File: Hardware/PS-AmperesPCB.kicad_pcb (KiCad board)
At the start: 2 copper layers, 70 x 60 mm, 45 parts, among them J1 Conn_01x04, J2 PeripheralCANConnector, J3 PeripheralCANConnector, U1 PeripheralSOM, U2 INA145UA/2K5, U3 AMC1300BDWV, U4 RO-123.3S_HP

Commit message: lay out lay out
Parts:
- removed +12V1, +3V3, +3V3H1, GND1, GNDH1, GNDPWR1, INN1, INP1, OUTN1, OUTP1, VOut1, aOut1: TestPoint, TestPoint:TestPoint_Keystone_5005-5009_Compact
- removed LOGO2: solarlogo, UTSVT_Special:UTSVT_Logo_Symbol
- removed REF**: Symbol_HighVoltage_Small, UTSVT_Special:Symbol_HighVoltage_Small
- added C11: 10uF, Capacitor_SMD:C_0805_2012Metric_Pad1.18x1.45mm_HandSolder, F.Cu at (99.9, 103.1)
- added C12: 10nF, Capacitor_SMD:C_0603_1608Metric_Pad1.08x0.95mm_HandSolder, F.Cu at (96.3, 101.0)
- added C13: 3.3nF, Capacitor_SMD:C_0603_1608Metric_Pad1.08x0.95mm_HandSolder, F.Cu at (108.7, 98.0)
- added C14: 0.1uF, Capacitor_SMD:C_0603_1608Metric_Pad1.08x0.95mm_HandSolder, F.Cu at (95.8, 111.8)
- added C15: 0.1uF, Capacitor_SMD:C_0603_1608Metric_Pad1.08x0.95mm_HandSolder, F.Cu at (96.6, 106.5)
- added C16: 1uF, Capacitor_SMD:C_0603_1608Metric_Pad1.08x0.95mm_HandSolder, F.Cu at (95.8, 109.0)
- added C17: 10uF, Capacitor_SMD:C_0805_2012Metric_Pad1.18x1.45mm_HandSolder, F.Cu at (101.9, 109.2)
- added C18: 10uF, Capacitor_SMD:C_0805_2012Metric_Pad1.18x1.45mm_HandSolder, F.Cu at (101.9, 113.5)
- added C19: 4.7uF, Capacitor_SMD:C_0805_2012Metric_Pad1.18x1.45mm_HandSolder, F.Cu at (106.7, 140.6)
- added C20: 100nF, Capacitor_SMD:C_0603_1608Metric_Pad1.08x0.95mm_HandSolder, F.Cu at (104.1, 140.7)
- added C21: 100nF, Capacitor_SMD:C_0603_1608Metric_Pad1.08x0.95mm_HandSolder, F.Cu at (101.6, 140.7)
- added C22: 100nF, Capacitor_SMD:C_0603_1608Metric_Pad1.08x0.95mm_HandSolder, F.Cu at (99.1, 140.7)
- added C23: 100nF, Capacitor_SMD:C_0603_1608Metric_Pad1.08x0.95mm_HandSolder, F.Cu at (88.5, 140.2)
- added C24: 100nF, Capacitor_SMD:C_0603_1608Metric_Pad1.08x0.95mm_HandSolder, F.Cu at (88.5, 141.9)
- added C25: 12p, Capacitor_SMD:C_0603_1608Metric_Pad1.08x0.95mm_HandSolder, F.Cu at (83.8, 133.7)
- added C26: 100nF, Capacitor_SMD:C_0603_1608Metric_Pad1.08x0.95mm_HandSolder, F.Cu at (88.5, 145.5)
- added C27: 12p, Capacitor_SMD:C_0603_1608Metric_Pad1.08x0.95mm_HandSolder, F.Cu at (83.8, 137.1)
- added C28: 100nF, Capacitor_SMD:C_0603_1608Metric_Pad1.08x0.95mm_HandSolder, F.Cu at (105.8, 148.5)
- added C29: 0.1uF, Capacitor_SMD:C_0603_1608Metric_Pad1.08x0.95mm_HandSolder, F.Cu at (95.2, 117.9)
- added C30: 100nF, Capacitor_SMD:C_0603_1608Metric_Pad1.08x0.95mm_HandSolder, F.Cu at (84.8, 127.8)
- added C31: 100nF, Capacitor_SMD:C_0603_1608Metric_Pad1.08x0.95mm_HandSolder, F.Cu at (86.6, 127.8)
- added C32: 4.7uF, Capacitor_SMD:C_0805_2012Metric_Pad1.18x1.45mm_HandSolder, F.Cu at (111.1, 118.6)
- added C33: 0.1uF, Capacitor_SMD:C_0603_1608Metric_Pad1.08x0.95mm_HandSolder, F.Cu at (104.5, 118.8)
- added C34: 10uF, Capacitor_SMD:C_0805_2012Metric_Pad1.18x1.45mm_HandSolder, F.Cu at (101.7, 117.9)
- added C35: 4.7uF, Capacitor_SMD:C_0805_2012Metric_Pad1.18x1.45mm_HandSolder, F.Cu at (105.5, 121.9)
- added C36: 0.1uF, Capacitor_SMD:C_0603_1608Metric_Pad1.08x0.95mm_HandSolder, F.Cu at (107.1, 118.8)
- added C37: 0.1uF, Capacitor_SMD:C_0603_1608Metric_Pad1.08x0.95mm_HandSolder, F.Cu at (100.1, 64.1)
- added C38: 1uF, Capacitor_SMD:C_0603_1608Metric_Pad1.08x0.95mm_HandSolder, F.Cu at (102.6, 64.1)
- added C39: 10uF, Capacitor_SMD:C_0805_2012Metric_Pad1.18x1.45mm_HandSolder, F.Cu at (112.0, 64.2)
- added C40: 0.1uF, Capacitor_SMD:C_0603_1608Metric_Pad1.08x0.95mm_HandSolder, F.Cu at (109.5, 64.1)
- added C41: 1uF, Capacitor_SMD:C_0603_1608Metric_Pad1.08x0.95mm_HandSolder, F.Cu at (124.5, 76.9)
- added C42: 0.1uF, Capacitor_SMD:C_0603_1608Metric_Pad1.08x0.95mm_HandSolder, F.Cu at (124.2, 64.4)
- added C43: 1nF, Capacitor_SMD:C_0603_1608Metric_Pad1.08x0.95mm_HandSolder, F.Cu at (126.4, 68.7)
- added C44: 7.5uF, Capacitor_SMD:C_0603_1608Metric_Pad1.08x0.95mm_HandSolder, F.Cu at (120.7, 76.9)
- added C45: 100nF, Capacitor_SMD:C_0603_1608Metric_Pad1.08x0.95mm_HandSolder, F.Cu at (128.9, 72.3)
- added C46: 1uF, Capacitor_SMD:C_0603_1608Metric_Pad1.08x0.95mm_HandSolder, F.Cu at (126.4, 72.3)
- added C47: 1uF, Capacitor_SMD:C_0603_1608Metric_Pad1.08x0.95mm_HandSolder, F.Cu at (110.7, 72.6)
- added C48: 100nF, Capacitor_SMD:C_0603_1608Metric_Pad1.08x0.95mm_HandSolder, F.Cu at (108.2, 72.6)
- added C49: 0.1uF, Capacitor_SMD:C_0603_1608Metric_Pad1.08x0.95mm_HandSolder, F.Cu at (131.2, 77.7)
- added C50: 10uF, Capacitor_SMD:C_0805_2012Metric_Pad1.18x1.45mm_HandSolder, F.Cu at (83.8, 91.7)
- added C51: 1uF, Capacitor_SMD:C_0603_1608Metric_Pad1.08x0.95mm_HandSolder, F.Cu at (83.5, 93.7)
- added C52: 1uF, Capacitor_SMD:C_0603_1608Metric_Pad1.08x0.95mm_HandSolder, F.Cu at (88.0, 91.4)
- added C53: 10uF, Capacitor_SMD:C_0805_2012Metric_Pad1.18x1.45mm_HandSolder, F.Cu at (87.9, 93.5)
- added C54: 100nF, Capacitor_SMD:C_0603_1608Metric_Pad1.08x0.95mm_HandSolder, F.Cu at (91.7, 97.5)
- added D10: Discharge, LED_SMD:LED_0603_1608Metric_Pad1.05x0.95mm_HandSolder, F.Cu at (100.0, 148.2)
- added D11: TVS, Diode_SMD:D_SOD-123F, F.Cu at (98.4, 118.4)
- added D12: CAN Status, LED_SMD:LED_0603_1608Metric_Pad1.05x0.95mm_HandSolder, F.Cu at (82.4, 130.7)
- added D13: 1N5819HW, Diode_SMD:D_SOD-123, F.Cu at (108.7, 122.8)
- added D14: SP0503BAHT, Package_TO_SOT_SMD:SOT-143, F.Cu at (107.0, 127.0)
- added D15: TVS, Diode_SMD:D_SOD-123F, F.Cu at (136.0, 79.1)
- added D16: TVS, Diode_SMD:D_SOD-123F, F.Cu at (136.0, 83.9)
- added D17: TVS, Diode_SMD:D_SOD-323_HandSoldering, F.Cu at (83.8, 89.4)
- added D18: TVS, Diode_SMD:D_SOD-123F, F.Cu at (87.6, 102.6)
- added D5: BUCK, LED_SMD:LED_0603_1608Metric_Pad1.05x0.95mm_HandSolder, F.Cu at (114.6, 175.0)
- added D6: MBR230S1F, Diode_SMD:D_SOD-123F, F.Cu at (105.2, 93.4)
- added D7: Heartbeat, LED_SMD:LED_0603_1608Metric_Pad1.05x0.95mm_HandSolder, F.Cu at (91.9, 148.2)
- added D8: Fault, LED_SMD:LED_0603_1608Metric_Pad1.05x0.95mm_HandSolder, F.Cu at (94.5, 148.1)
- added D9: Charge, LED_SMD:LED_0603_1608Metric_Pad1.05x0.95mm_HandSolder, F.Cu at (97.3, 148.1)
- added FB1: FerriteBead, Capacitor_SMD:C_0603_1608Metric_Pad1.08x0.95mm_HandSolder, F.Cu at (88.4, 147.5)
- added FB2: FerriteBead, Capacitor_SMD:C_0603_1608Metric_Pad1.08x0.95mm_HandSolder, F.Cu at (88.5, 143.7)
- added H1: M1, MountingHole:MountingHole_3.2mm_M3_DIN965_Pad_TopBottom, F.Cu at (20.1, 20.8)
- added H2: M3, MountingHole:MountingHole_3.2mm_M3_DIN965_Pad_TopBottom, F.Cu at (20.1, 27.9)
- added H3: M2, MountingHole:MountingHole_3.2mm_M3_DIN965_Pad_TopBottom, F.Cu at (20.1, 35.1)
- added H4: M4, MountingHole:MountingHole_3.2mm_M3_DIN965_Pad_TopBottom, F.Cu at (20.1, 42.2)
- added IC1: SN74AHC1G32DBVR, Parts:SN74AHC1G32DBVR, F.Cu at (91.2, 118.9)
- added IC2: INA241A4IDR, Parts:INA241A5IDR, F.Cu at (118.4, 63.9)
- added IC3: AMC1350DWVR, Parts:AMC1350DWVR, F.Cu at (118.8, 69.9)
- added IC4: TLV9002QDRQ1, Parts:TLV9002QDRQ1, F.Cu at (129.3, 81.6)
- added IC5: LM76202QPWPRQ1, UTSVT_Power:LM76202QPWPRQ1, F.Cu at (85.9, 97.5)
- added J4: Conn_01x02_Pin, Connector_PinHeader_2.54mm:PinHeader_1x02_P2.54mm_Vertical, F.Cu at (95.5, 125.2)
- added J5: USB4120-03-C, Parts:USB412003C, F.Cu at (105.5, 133.0)
- added J6: Scrut Conn, Connector_Molex:Molex_Nano-Fit_105309-xx02_1x02_P2.50mm_Vertical, F.Cu at (73.2, 60.7)
- added JP1: Termination, Connector_PinHeader_2.54mm:PinHeader_1x02_P2.54mm_Vertical, F.Cu at (81.0, 123.9)
- added L1: 100uH, Inductor_SMD:L_Coilcraft_MSS1246-XXX, F.Cu at (117.3, 99.0)
- added PS1: 1769205341, Parts:WE_1769205341, F.Cu at (89.8, 60.9)
- added R10: 10K, Resistor_SMD:R_0603_1608Metric_Pad0.98x0.95mm_HandSolder, F.Cu at (107.8, 148.5)
- added R11: 120, Resistor_SMD:R_0603_1608Metric_Pad0.98x0.95mm_HandSolder, F.Cu at (91.9, 144.4)
- added R12: 120, Resistor_SMD:R_0603_1608Metric_Pad0.98x0.95mm_HandSolder, F.Cu at (94.5, 144.4)
- added R13: 120, Resistor_SMD:R_0603_1608Metric_Pad0.98x0.95mm_HandSolder, F.Cu at (97.3, 144.4)
- added R14: 120, Resistor_SMD:R_0603_1608Metric_Pad0.98x0.95mm_HandSolder, F.Cu at (100.1, 144.5)
- added R15: 10k, Resistor_SMD:R_0603_1608Metric_Pad0.98x0.95mm_HandSolder, F.Cu at (95.4, 119.9)
- added R16: 120, Resistor_SMD:R_0603_1608Metric_Pad0.98x0.95mm_HandSolder, F.Cu at (85.8, 130.7)
- added R17: 10k, Resistor_SMD:R_0603_1608Metric_Pad0.98x0.95mm_HandSolder, F.Cu at (89.4, 130.7)
- added R18: 120, Resistor_SMD:R_0603_1608Metric_Pad0.98x0.95mm_HandSolder, F.Cu at (87.1, 123.9)
- added R19: 1k, Resistor_SMD:R_0603_1608Metric_Pad0.98x0.95mm_HandSolder, F.Cu at (108.9, 118.6)
- added R20: 22k, Resistor_SMD:R_0603_1608Metric_Pad0.98x0.95mm_HandSolder, F.Cu at (101.6, 120.1)
- added R21: 47k, Resistor_SMD:R_0603_1608Metric_Pad0.98x0.95mm_HandSolder, F.Cu at (101.6, 121.9)
- added R22: 5.1k, Resistor_SMD:R_0603_1608Metric_Pad0.98x0.95mm_HandSolder, F.Cu at (109.6, 127.0)
- added R23: 5.1k, Resistor_SMD:R_0603_1608Metric_Pad0.98x0.95mm_HandSolder, F.Cu at (111.5, 127.0)
- added R24: Shunt, Parts:WSBS8518L2500JK, F.Cu at (95.0, 33.5)
- added R25: 8.2k, Resistor_SMD:R_0603_1608Metric_Pad0.98x0.95mm_HandSolder, F.Cu at (126.3, 76.9)
- added R26: 3.3k, Resistor_SMD:R_0603_1608Metric_Pad0.98x0.95mm_HandSolder, F.Cu at (110.9, 68.7)
- added R27: 4.3k, Resistor_SMD:R_0603_1608Metric_Pad0.98x0.95mm_HandSolder, F.Cu at (122.6, 76.9)
- added R28: 34k, Resistor_SMD:R_0603_1608Metric_Pad0.98x0.95mm_HandSolder, F.Cu at (77.2, 60.7)
- added R29: 51, Resistor_SMD:R_0603_1608Metric_Pad0.98x0.95mm_HandSolder, F.Cu at (77.2, 63.5)
- added R30: 100k, Resistor_SMD:R_0603_1608Metric_Pad0.98x0.95mm_HandSolder, F.Cu at (91.7, 102.6)
- added R31: 24m, Resistor_SMD:R_0603_1608Metric_Pad0.98x0.95mm_HandSolder, F.Cu at (91.7, 100.8)
- added R32: 10k, Resistor_SMD:R_0603_1608Metric_Pad0.98x0.95mm_HandSolder, F.Cu at (91.7, 99.1)
- added R33: 10k, Resistor_SMD:R_0603_1608Metric_Pad0.98x0.95mm_HandSolder, F.Cu at (90.9, 95.0)
- added R34: 10k, Resistor_SMD:R_0603_1608Metric_Pad0.98x0.95mm_HandSolder, F.Cu at (83.6, 102.6)
- added R35: 402k, Resistor_SMD:R_0603_1608Metric_Pad0.98x0.95mm_HandSolder, F.Cu at (79.9, 100.3)
- added R36: 45.3k, Resistor_SMD:R_0603_1608Metric_Pad0.98x0.95mm_HandSolder, F.Cu at (79.9, 94.5)
- added R37: 590, Resistor_SMD:R_0603_1608Metric_Pad0.98x0.95mm_HandSolder, F.Cu at (79.9, 96.5)
- added R38: 2.1k, Resistor_SMD:R_0603_1608Metric_Pad0.98x0.95mm_HandSolder, F.Cu at (79.9, 98.5)
- added SW1: RST, Parts:SW_TL3365AF180QG, F.Cu at (106.9, 144.8)
- added SW2: BOOT, Parts:SW_CJS-1200TA, F.Cu at (85.5, 118.6)
- added SW3: Scrut Select, Button_Switch_SMD:SW_DPDT_CK_JS202011JCQN, F.Cu at (118.5, 55.9)
- added TP1: TP_Current, TestPoint:TestPoint_Pad_1.0x1.0mm, F.Cu at (19.8, 51.5)
- added TP10: SHUNT+, TestPoint:TestPoint_Pad_1.0x1.0mm, F.Cu at (158.8, 52.8)
- added TP11: SHUNT-, TestPoint:TestPoint_Pad_1.0x1.0mm, F.Cu at (162.8, 52.8)
- added TP12: V_In+, TestPoint:TestPoint_Pad_1.0x1.0mm, F.Cu at (166.8, 52.8)
- added TP13: V_Out+, TestPoint:TestPoint_Pad_1.0x1.0mm, F.Cu at (170.8, 52.8)
- added TP14: V_In-, TestPoint:TestPoint_Pad_1.0x1.0mm, F.Cu at (174.8, 52.8)
- added TP2: 24V_Ext, TestPoint:TestPoint_Pad_1.0x1.0mm, F.Cu at (159.3, 112.5)
- added TP3: 24V, TestPoint:TestPoint_Pad_1.0x1.0mm, F.Cu at (159.3, 115.6)
- added TP4: 3V3_HV, TestPoint:TestPoint_Pad_1.0x1.0mm, F.Cu at (162.3, 112.5)
- added TP5: 3V3, TestPoint:TestPoint_Pad_1.0x1.0mm, F.Cu at (162.3, 115.6)
- added TP6: 5V_BK, TestPoint:TestPoint_Pad_1.0x1.0mm, F.Cu at (165.4, 112.5)
- added TP7: 5V_USB, TestPoint:TestPoint_Pad_1.0x1.0mm, F.Cu at (165.4, 115.6)
- added TP8: GND, TestPoint:TestPoint_Pad_1.0x1.0mm, F.Cu at (170.5, 114.1)
- added TP9: GND HV, TestPoint:TestPoint_Pad_1.0x1.0mm, F.Cu at (174.5, 114.1)
- added U5: STM32L431CBTx, Package_QFP:LQFP-48_7x7mm_P0.5mm, F.Cu at (94.6, 135.6)
- added U6: TCAN337, UTSVT_ICs:TCAN337DCNR, F.Cu at (90.5, 127.7)
- added U7: CDSOT23-T24CAN, UTSVT_ICs:CDSOT23-T24CAN, F.Cu at (91.2, 123.4)
- added U8: CP2102N-A02-GQFN24, UTSVT_ICs:CP2102N-A02-GQFN24, F.Cu at (102.5, 125.7)
- added U9: REF35125QDBVR, Package_TO_SOT_SMD:SOT-23-6, F.Cu at (106.1, 64.2)
- added Y1: 8M, Crystal:Crystal_SMD_Abracon_ABM3-2Pin_5.0x3.2mm, F.Cu at (87.0, 135.4)
- C1: value 1uF -> 4.7uF; footprint Capacitor_SMD:C_0805_2012Metric -> Capacitor_SMD:C_0805_2012Metric_Pad1.18x1.45mm_HandSolder
- C10, C3: value 1uF -> 10uF; footprint Capacitor_SMD:C_0805_2012Metric -> Capacitor_SMD:C_0805_2012Metric_Pad1.18x1.45mm_HandSolder
- C2: value 2.2uF -> 4.7uF; footprint Capacitor_SMD:C_0805_2012Metric -> Capacitor_SMD:C_0805_2012Metric_Pad1.18x1.45mm_HandSolder
- C4: value 1n -> 10uF; footprint Capacitor_SMD:C_0805_2012Metric -> Capacitor_SMD:C_0805_2012Metric_Pad1.18x1.45mm_HandSolder
- C5: value 10u -> 10uF; footprint Capacitor_SMD:C_0805_2012Metric -> Capacitor_SMD:C_0805_2012Metric_Pad1.18x1.45mm_HandSolder
- C6: value 2.2n -> 0.1uF; footprint Capacitor_SMD:C_0805_2012Metric -> Capacitor_SMD:C_0603_1608Metric_Pad1.08x0.95mm_HandSolder
- C7: value 2.2uF -> 10uF; footprint Capacitor_SMD:C_0805_2012Metric -> Capacitor_SMD:C_0805_2012Metric_Pad1.18x1.45mm_HandSolder
- C8: value 2.2uF -> 1uF; footprint Capacitor_SMD:C_0805_2012Metric -> Capacitor_SMD:C_0603_1608Metric_Pad1.08x0.95mm_HandSolder
- C9: footprint Capacitor_SMD:C_0805_2012Metric -> Capacitor_SMD:C_0805_2012Metric_Pad1.18x1.45mm_HandSolder
- D1: value PowerOn -> 24V; footprint LED_SMD:LED_0805_2012Metric -> LED_SMD:LED_0603_1608Metric_Pad1.05x0.95mm_HandSolder
- D2: value RBE01VYM6AFHTR -> 3.3V HV; footprint Parts:RBE01VYM6AFHTR -> LED_SMD:LED_0603_1608Metric_Pad1.05x0.95mm_HandSolder
- D3: value RBE01VYM6AFHTR -> 3.3V; footprint Parts:RBE01VYM6AFHTR -> LED_SMD:LED_0603_1608Metric_Pad1.05x0.95mm_HandSolder
- D4: value PowerOn -> PFLT; footprint LED_SMD:LED_0805_2012Metric -> LED_SMD:LED_0603_1608Metric_Pad1.05x0.95mm_HandSolder
- J1: value Conn_01x04 -> PeripheralCAN; footprint Connector_PinSocket_2.54mm:PinSocket_1x04_P2.54mm_Vertical -> UTSVT_Connectors:Molex_Nano-Fit_105309-xx04_1x04_P2.50mm_Vertical
- J2: value PeripheralCANConnector -> PeripheralCAN; footprint UTSVT_Connectors:Molex_MicroFit3.0_1x4xP3.00mm_PolarizingPeg_Vertical -> UTSVT_Connectors:Molex_Nano-Fit_105309-xx04_1x04_P2.50mm_Vertical
- J3: value PeripheralCANConnector -> SWD; footprint UTSVT_Connectors:Molex_MicroFit3.0_1x4xP3.00mm_PolarizingPeg_Vertical -> Connector_Molex:Molex_Nano-Fit_105309-xx04_1x04_P2.50mm_Vertical
- LOGO1: value aniMegamind -> logo placeholder; footprint Parts:aniMegamind -> UTSVT_Logos:LHRs_LOGO; moved to F.Cu
- R1, R4: value 2.4k -> 4.3k; footprint Resistor_SMD:R_0805_2012Metric -> Resistor_SMD:R_0603_1608Metric_Pad0.98x0.95mm_HandSolder
- R2, R3: value 2.4k -> 120; footprint Resistor_SMD:R_0805_2012Metric -> Resistor_SMD:R_0603_1608Metric_Pad0.98x0.95mm_HandSolder
- R5: value 1.5k -> 768; footprint Resistor_SMD:R_0805_2012Metric -> Resistor_SMD:R_0603_1608Metric_Pad0.98x0.95mm_HandSolder
- R6: value 12k -> 16k; footprint Resistor_SMD:R_0805_2012Metric -> Resistor_SMD:R_0603_1608Metric_Pad0.98x0.95mm_HandSolder
- R7: value 1k -> ROSC; footprint Resistor_SMD:R_0805_2012Metric -> Resistor_SMD:R_0603_1608Metric_Pad0.98x0.95mm_HandSolder
- R8: value 4.8k -> 10k; footprint Resistor_SMD:R_0805_2012Metric -> Resistor_SMD:R_0603_1608Metric_Pad0.98x0.95mm_HandSolder
- R9: value 1.5k -> 332; footprint Resistor_SMD:R_0805_2012Metric -> Resistor_SMD:R_0603_1608Metric_Pad0.98x0.95mm_HandSolder
- U1: value PeripheralSOM -> LT1963AEST-3.3#TRPBF; footprint UTSVT_Special:PeripheralSOM -> Package_TO_SOT_SMD:SOT-223-3_TabPin2
- U2: value INA145UA/2K5 -> TPS5405DR; footprint Parts:D8 -> UTSVT_Power:TPS5405DR
- U3: value AMC1300BDWV -> TPS2115ADRBR; footprint Package_SO:SOIC-8_7.5x5.85mm_P1.27mm -> Package_SON:VSON-8-1EP_3x3mm_P0.65mm_EP1.65x2.4mm
- U4: value RO-123.3S_HP -> LT1963AEST-3.3#TRPBF; footprint UTSVT_ICs:RI3_DC_Converter -> Package_TO_SOT_SMD:SOT-223-3_TabPin2
- moved D4 119.9 mm to (114.6, 172.2)
- moved R5 117.5 mm to (110.1, 174.9)
- moved R2 112.2 mm to (110.1, 167.4), turned to 0 degrees
- moved D1 112.1 mm to (114.6, 164.8), turned to 180 degrees
- moved R4 106.1 mm to (110.1, 172.2), turned to 0 degrees
- moved R1 103.9 mm to (110.1, 164.8), turned to 0 degrees
- moved R3 103.3 mm to (110.1, 169.9), turned to 0 degrees
- moved D2 99.2 mm to (114.6, 167.3)
- moved D3 98.4 mm to (114.6, 169.9), turned to 180 degrees
- moved LOGO1 95.2 mm to (32.3, 20.8), turned to 0 degrees
- moved J3 91.8 mm to (70.1, 124.2)
- moved J2 71.4 mm to (70.1, 108.3)
- moved U4 70.9 mm to (107.6, 110.4)
- moved R9 69.0 mm to (92.0, 111.8), turned to 0 degrees
- moved J1 64.4 mm to (70.1, 93.7), turned to 0 degrees
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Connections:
- C1 pad 1: +3V3 High -> +24V
- C1 pad 2: GND High -> GND
- C10 pad 1: +3V3 -> +5V_BUCK
- C2 pad 1: /INP -> +24V
- C2 pad 2: /INN -> GND
- C3 pad 1: +3V3 -> +5V HV
- C3 pad 2: GND -> GND HV
- C4 pad 1: +12V -> +5V HV
- C4 pad 2: GNDPWR -> GND HV
- C5 pad 1: +12V -> +3.3V HV
- C5 pad 2: GNDPWR -> GND HV
- C6 pad 1: GNDPWR -> Net-(U2-BOOT)
- C6 pad 2: GND High -> Net-(D6-K)
- C7 pad 1: Net-(U2-V-IN) -> +24V
- C7 pad 2: Net-(U2-V+IN) -> GND
- C8 pad 1: /aOut -> +24V
- C9 pad 1: +3V3 High -> +5V_BUCK
- C9 pad 2: GND High -> GND
- D2 pad 1: +3V3 -> GND HV
- D3 pad 1: Net-(D2-A) -> GND
- D3 pad 2: GND -> Net-(D3-A)
- D4 pad 1: GND High -> /Power/PWR_Fault
- J1 pad 1: Net-(J1-Pin_1) -> +24V_Ext
- J1 pad 2: GND High -> GND
- J1 pad 3: GND High -> /CAN_HIGH
- J1 pad 4: +3V3 High -> /CAN_LOW
- J2 pad 1: +12V -> +24V_Ext
- J2 pad 2: GNDPWR -> GND
- J2 pad 3: Net-(J2-CAN_H) -> /CAN_HIGH
- J2 pad 4: Net-(J2-CAN_L) -> /CAN_LOW
- J3 pad 1: +12V -> +3.3V
- J3 pad 2: GNDPWR -> /MCU/SWCLK
- J3 pad 3: Net-(J2-CAN_H) -> GND
- J3 pad 4: Net-(J2-CAN_L) -> /MCU/SWDIO
- R1 pad 1: /INP -> +24V
- R1 pad 2: Net-(J1-Pin_1) -> Net-(D1-A)
- R2 pad 1: /INN -> +3.3V HV
- R2 pad 2: GND High -> Net-(D2-A)
- R3 pad 1: Net-(U2-V-IN) -> +3.3V
- R3 pad 2: /OUTN -> Net-(D3-A)
- R4 pad 1: Net-(U2-V+IN) -> +24V
- R4 pad 2: /OUTP -> Net-(D4-A)
- R5 pad 1: +3V3 -> +5V_BUCK
- R5 pad 2: Net-(D1-A) -> Net-(D5-A)
- R6 pad 1: Net-(D2-A) -> Net-(C13-Pad2)
- R6 pad 2: Net-(U2-RG) -> GND
- R7 pad 1: Net-(U2-RG) -> /Power/ROSC
- R8 pad 1: /aOut -> +5V
- R8 pad 2: Net-(D2-A) -> /Power/STAT
- R9 pad 1: +3V3 High -> /Power/ILIM
- R9 pad 2: Net-(D4-A) -> GND
- U1 pad 1: unconnected-(U1-SPI2_MOSI-Pad1) -> +5V HV
- U1 pad 2: +3V3 -> GND HV
- U1 pad 3: unconnected-(U1-SPI2_MISO-Pad3) -> +3.3V HV
- U2 pad 1: GND -> Net-(U2-BOOT)
- U2 pad 2: Net-(U2-V-IN) -> +24V
- U2 pad 3: Net-(U2-V+IN) -> /Power/ROSC
- U2 pad 4: GND -> Net-(U2-SS)
- U2 pad 5: Net-(U2-RG) -> +5V_BUCK
- U2 pad 6: Net-(D2-A) -> Net-(U2-COMP)
- U2 pad 7: +3V3 -> GND
- U2 pad 8: unconnected-(U2-VO1-Pad8) -> Net-(D6-K)
- U3 pad 1: +3V3 High -> /Power/STAT
- U3 pad 2: /INP -> unconnected-(U3-D0-Pad2)
- U3 pad 3: /INN -> GND
- U3 pad 4: GND High -> /Power/ILIM
- U3 pad 6: /OUTN -> +5V_VBUS
- U3 pad 7: /OUTP -> +5V
- U3 pad 8: +3V3 -> +5V_BUCK
- U4 pad 1: GNDPWR -> +5V
- U4 pad 2: +12V -> GND
- U4 pad 3: GND High -> +3.3V
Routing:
- net +3V3: track 82.3 -> 0.00 mm
- net +12V: track 69.9 -> 0.00 mm, vias 2 -> 0
- net +3V3 High: track 52.4 -> 0.00 mm, vias 2 -> 0
- net /OUTN: track 52.2 -> 0.00 mm
- net /aOut: track 51.4 -> 0.00 mm, vias 2 -> 0
- net /INP: track 47.7 -> 0.00 mm
- net /INN: track 39.0 -> 0.00 mm
- net /OUTP: track 38.9 -> 0.00 mm
- net Net-(J2-CAN_L): track 38.0 -> 0.00 mm
- net Net-(J2-CAN_H): track 36.2 -> 0.00 mm
- net Net-(D2-A): track 31.0 -> 0.00 mm
- net Net-(J1-Pin_1): track 24.8 -> 0.00 mm, vias 2 -> 0
- net Net-(U2-V+IN): track 7.58 -> 0.00 mm
- net Net-(U2-RG): track 5.75 -> 0.00 mm
- net Net-(U2-V-IN): track 5.43 -> 0.00 mm
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- removed copper zone on B.Cu, net GND
- removed copper zone on F.Cu, net GND
- removed copper zone on B.Cu, net GND High
- removed copper zone on F.Cu, net GND High
- removed copper zone on B.Cu, net GNDPWR
- removed copper zone on F.Cu, net GNDPWR
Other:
- board outline removed
- board text removed: "+12V"
- board text removed: "+3V3"
- board text removed: "+3V3 High"
- board text removed: "3v3 High"
- board text removed: "CAN_H"
- board text removed: "CAN_L"
- board text removed: "Fusebox"
- board text removed: "GND"
- board text removed: "GND High"
- board text removed: "GNDPWR"
- board text removed: "Hey!"
- board text removed: "High Voltage Power"
- board text removed: "IN"
- board text removed: "INN"
- board text removed: "INP"
- board text removed: "LHR Solar: Amperes Board By: Nathan and Aniruddh"
- board text removed: "OUT"
- board text removed: "OUTN"
- board text removed: "OUTP"
- board text removed: "aOut"
- board text removed: "aOut (unfiltered)"

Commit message: changed shunt model, moved around folders; initial layout, routing soon
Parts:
- removed R24: Shunt, Parts:WSBS8518L2500JK
- added R39: WSBS8518L2500JTP3, Parts:WSBS8518L2500JKM4, F.Cu at (192.1, 47.2)
- moved H4 260.8 mm to (271.5, 111.3)
- moved H1 251.9 mm to (271.8, 30.7)
- moved TP1 222.9 mm to (242.5, 61.4)
- moved H2 209.8 mm to (229.9, 31.0)
- moved R2 200.5 mm to (273.5, 51.1), turned to 90 degrees
- moved D2 198.9 mm to (273.5, 47.5), turned to -90 degrees
- moved H3 196.4 mm to (201.2, 111.0)
- moved J6 193.9 mm to (264.8, 31.1), turned to -90 degrees
- moved J3 193.2 mm to (263.0, 112.7), turned to -90 degrees
- moved FB1 190.1 mm to (271.2, 95.3), turned to -90 degrees
- moved R28 189.7 mm to (265.1, 34.4)
- moved D7 188.5 mm to (271.8, 91.8), turned to 180 degrees
- moved C26 187.5 mm to (269.2, 95.2), turned to 90 degrees
- moved D8 186.8 mm to (271.8, 89.2), turned to 180 degrees
- moved R29 186.6 mm to (261.5, 34.4), turned to 0 degrees
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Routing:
- added copper zone on F.Cu, net +3.3V
- added copper zone on F.Cu, net +3.3V HV
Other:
- board text added: "For Instructional Use Only."
- board text added: "SOLIDWORKS Educational Product."

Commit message: 9/20 workday: some layout stuff ye ye
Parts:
- moved D1 72.5 mm to (273.0, 71.8), turned to 180 degrees
- moved D5 72.3 mm to (273.0, 82.0), turned to 180 degrees
- moved D3 71.8 mm to (273.0, 75.2), turned to 180 degrees
- moved D4 71.7 mm to (273.0, 78.6), turned to 180 degrees
- moved TP6 66.2 mm to (263.2, 111.7), turned to 0 degrees
- moved R1 63.6 mm to (268.5, 72.0), turned to 0 degrees
- moved R5 63.3 mm to (268.5, 82.0), turned to 0 degrees
- moved R3 62.8 mm to (268.5, 75.3), turned to 0 degrees
- moved R4 62.7 mm to (268.5, 78.7), turned to 0 degrees
- moved TP8 61.1 mm to (259.0, 111.7), turned to 0 degrees
- moved TP2 56.1 mm to (254.7, 111.7), turned to 0 degrees
- moved J3 55.3 mm to (271.9, 58.1), turned to 0 degrees
- moved TP7 51.1 mm to (250.5, 111.7), turned to 0 degrees
- moved J4 49.1 mm to (202.5, 104.3), turned to -90 degrees
- moved JP1 47.6 mm to (200.0, 99.7), turned to 90 degrees
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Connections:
- R39 pad 1: /Current Sense/SHUNT+ -> /Current Sense/SHUNT-
- R39 pad 2: /Current Sense/SHUNT- -> /Current Sense/SHUNT+
- R39 pad MH1: unconnected-(R39-PadMH1) -> /Current Sense/Battery_GND
- R39 pad MH2: unconnected-(R39-PadMH2) -> /Current Sense/Output_GND
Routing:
- added copper zone on F.Cu, net +24V
- added copper zone on F.Cu, net +24V_Ext
- added copper zone on F.Cu, net +5V
- added copper zone on F.Cu, net +5V HV
- added copper zone on F.Cu, net +5V_BUCK
- added copper zone on F.Cu, net /Power/PowerProtection/RTN
- added copper zone on F.Cu, net Net-(D6-K)
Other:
- board text added: "AAHAHAH"
- board text added: "footprint for dpdt switch??"

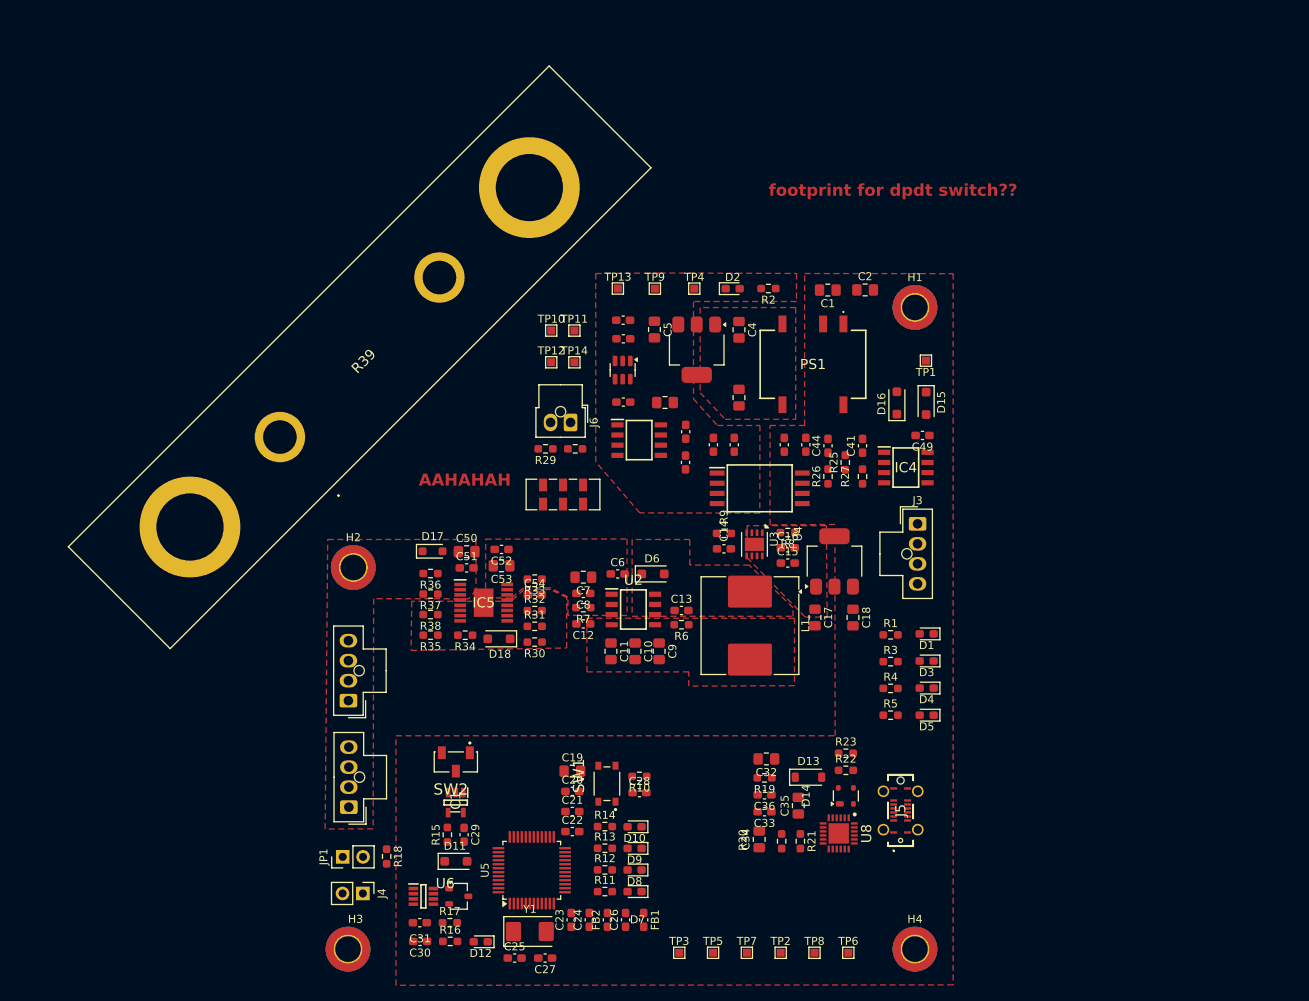
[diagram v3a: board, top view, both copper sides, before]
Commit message: better layout, started routing
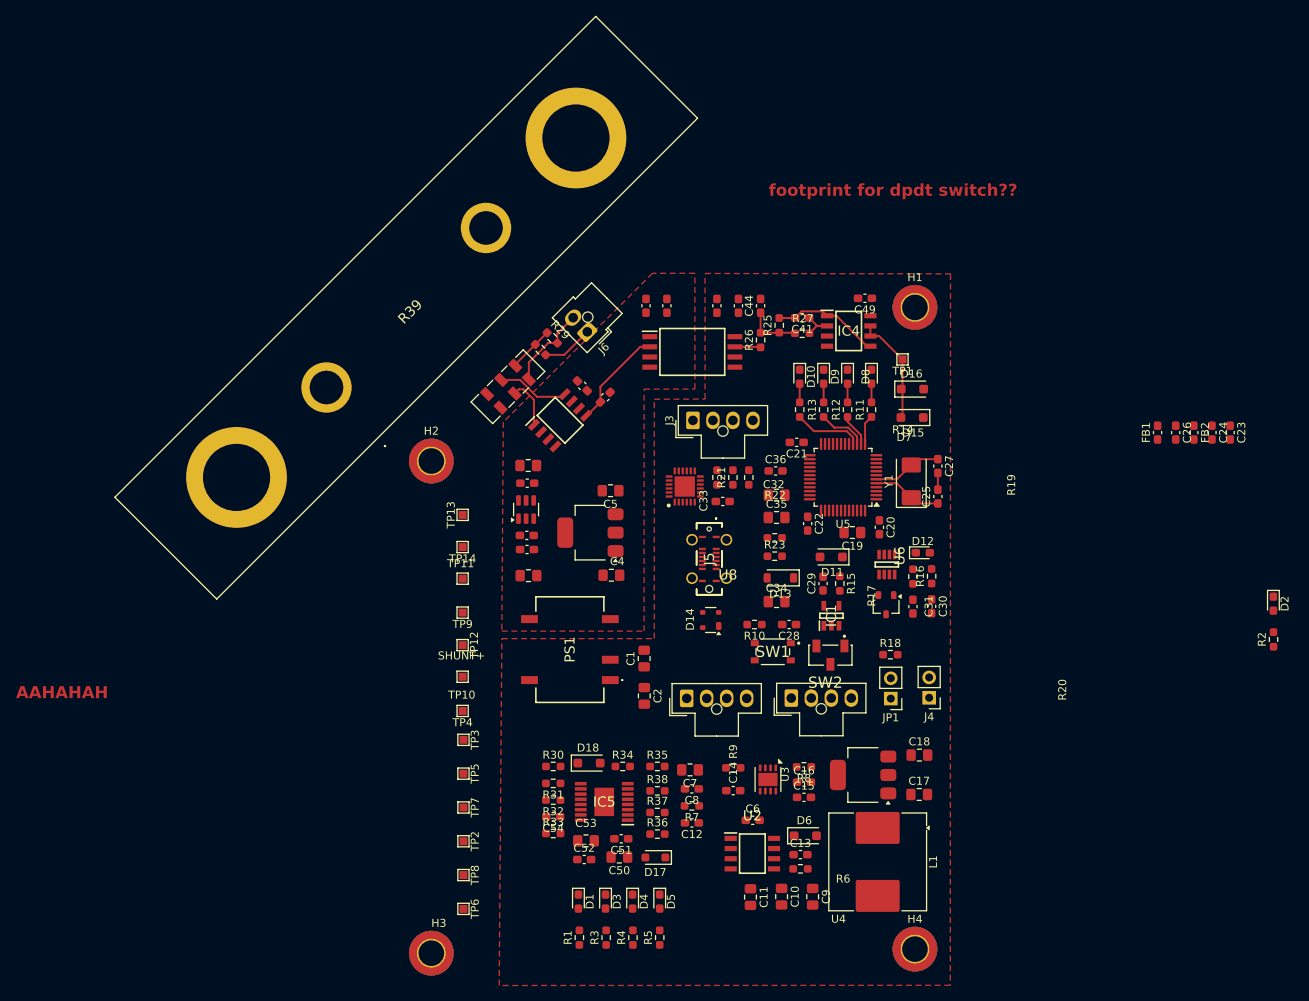
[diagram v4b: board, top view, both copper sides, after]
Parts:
- moved C23 102.4 mm to (310.9, 46.7), turned to -90 degrees
- moved C24 98.8 mm to (308.7, 46.7), turned to -90 degrees
- moved FB2 95.3 mm to (306.4, 46.7), turned to -90 degrees
- moved C26 91.9 mm to (304.1, 46.7), turned to -90 degrees
- moved FB1 88.5 mm to (301.9, 46.7), turned to 90 degrees
- moved C27 78.7 mm to (274.4, 50.9), turned to -90 degrees
- moved C25 78.3 mm to (274.4, 54.7), turned to 90 degrees
- moved D2 78.2 mm to (316.3, 68.1), turned to -90 degrees
- moved R2 76.9 mm to (316.3, 72.5), turned to 90 degrees
- moved C30 76.4 mm to (273.6, 68.4), turned to -90 degrees
- moved R16 75.5 mm to (273.6, 64.6), turned to 90 degrees
- moved J4 74.9 mm to (273.3, 79.8), turned to 180 degrees
- moved Y1 73.8 mm to (271.1, 52.8), turned to 90 degrees
- moved D12 73.6 mm to (272.5, 61.7), turned to 0 degrees
- moved C31 73.2 mm to (271.3, 68.4), turned to -90 degrees
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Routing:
- net /Current Sense/I_OUT: track 0.00 -> 13.8 mm
- net /Current Sense/OUT1: track 0.00 -> 13.5 mm
- net /Current Sense/SENSE+: track 0.00 -> 12.6 mm
- net /Current Sense/Scrut-: track 0.00 -> 10.7 mm
- net /Current Sense/INPUT+: track 0.00 -> 8.95 mm
- net /MCU/OSC_IN: track 0.00 -> 8.73 mm
- net /MCU/OSC_OUT: track 0.00 -> 8.73 mm
- net /MCU/LED_DISCHARGE: track 0.00 -> 8.54 mm
- net Net-(C44-Pad1): track 0.00 -> 6.82 mm
- net /Current Sense/Scrut+: track 0.00 -> 6.40 mm
- net /Current Sense/INPUT-: track 0.00 -> 6.29 mm
- net /MCU/LED_CHARGE: track 0.00 -> 6.13 mm
- net /Current Sense/Scrut_Out: track 0.00 -> 5.78 mm
- net Net-(IC4-IN1-): track 0.00 -> 5.23 mm
- net /MCU/LED_FAULT: track 0.00 -> 4.07 mm
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- added copper zone on F.Cu, net GND
- added copper zone on F.Cu, net GND HV
- removed copper zone on F.Cu, net +24V
- removed copper zone on F.Cu, net +24V_Ext
- removed copper zone on F.Cu, net +3.3V
- removed copper zone on F.Cu, net +3.3V HV
- removed copper zone on F.Cu, net +5V
- removed copper zone on F.Cu, net +5V HV
- removed copper zone on F.Cu, net +5V_BUCK
- removed copper zone on F.Cu, net /Power/PowerProtection/RTN
- removed copper zone on F.Cu, net Net-(D6-K)

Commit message: board is smaller ? idk
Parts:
- C23, C24, C26, C32, C33, C35, C36, FB1, FB2, R22, R23: moved to B.Cu
- SW3: value Scrut Select -> Scrutineering
- moved D2 166.4 mm to (150.2, 77.3)
- moved R2 166.4 mm to (150.2, 81.0)
- moved J2 138.9 mm to (128.0, 125.9), turned to 180 degrees
- moved C23 136.8 mm to (178.8, 81.8)
- moved C24 133.0 mm to (180.4, 81.8)
- moved FB2 131.8 mm to (180.4, 85.2), turned to 90 degrees
- moved C26 131.7 mm to (177.2, 81.8)
- moved FB1 131.0 mm to (175.7, 81.8), turned to -90 degrees
- moved J1 122.4 mm to (128.0, 112.4), turned to 180 degrees
- moved R35 107.4 mm to (138.5, 125.2), turned to 180 degrees
- moved R38 105.7 mm to (138.5, 122.9), turned to 180 degrees
- moved R37 104.3 mm to (138.5, 120.9), turned to 180 degrees
- moved R36 103.2 mm to (138.5, 118.6), turned to 180 degrees
- moved D17 101.6 mm to (138.7, 115.7), turned to 0 degrees
- moved C17 100.3 mm to (173.1, 107.9)
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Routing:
- net /MCU/NRST: track 0.00 -> 18.2 mm
- net /Current Sense/I_OUT: track 13.8 -> 29.9 mm
- net /CAN_HIGH: track 0.00 -> 12.7 mm
- net +1V25: track 0.00 -> 9.20 mm
- net /USB/D+: track 0.00 -> 8.99 mm
- net /USB/D-: track 0.00 -> 8.97 mm
- net /Current Sense/INPUT+: track 8.95 -> 0.00 mm
- net /MCU/BOOT0: track 0.00 -> 8.45 mm
- net /Current Sense/Scrut-: track 10.7 -> 3.99 mm
- net /Current Sense/Scrut+: track 6.40 -> 0.00 mm
- net /Current Sense/INPUT-: track 6.29 -> 0.00 mm
- net /Power/PowerProtection/UVLO: track 0.00 -> 6.15 mm
- net /USB/VBUS_IN: track 0.00 -> 5.96 mm
- net /Power/PowerProtection/IMON: track 0.00 -> 5.94 mm
- net /Power/PowerProtection/OVP: track 0.00 -> 5.62 mm
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- added copper zone on F.Cu, net +24V
- added copper zone on F.Cu, net +24V_Ext
- added copper zone on F.Cu, net +5V
- added copper zone on F.Cu, net +5V HV
- added copper zone on F.Cu, net +5V_BUCK
- added copper zone on F.Cu, net Net-(D6-K)
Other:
- board outline added: 68.9 x 82.5 mm
